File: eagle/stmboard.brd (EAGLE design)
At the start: 62.2 x 57.1 mm, 23 parts, among them IC1 LD117AS12TR

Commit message: fixed arduino header spacing
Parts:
- moved JP6 2.03 mm to (34.7, -5.71)
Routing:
- net PA10_SDA: track 42.4 -> 40.1 mm
- net GND: track 11.6 -> 13.9 mm
- net PA9_SCL_BTN: track 48.1 -> 47.3 mm
- net PA5_SCK_LED: track 50.0 -> 50.5 mm
- net PA8_PWM: track 25.7 -> 26.2 mm
- net PA7_MOSI: track 40.3 -> 40.8 mm
- net PB0_PWM: track 36.7 -> 37.3 mm
- net PA6_MISO: track 43.8 -> 44.4 mm
- net PA11: track 23.6 -> 23.1 mm
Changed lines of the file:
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@@
 <attribute name="VALUE" x="69.215" y="-2.54" size="1.27" layer="27" rot="R180"/>
 </element>
-<element name="JP6" library="pinhead" library_urn="urn:adsk.eagle:library:325" package="1X10" package3d_urn="urn:adsk.eagle:package:22406/2" value="" x="32.639" y="-5.715" locked="yes" smashed="yes" rot="R180">
-<attribute name="NAME" x="45.4152" y="-7.5438" size="1.27" layer="25" ratio="10" rot="R180"/>
-<attribute name="VALUE" x="45.339" y="-2.54" size="1.27" layer="27" rot="R180"/>
+<element name="JP6" library="pinhead" library_urn="urn:adsk.eagle:library:325" package="1X10" package3d_urn="urn:adsk.eagle:package:22406/2" value="" x="34.671" y="-5.715" smashed="yes" rot="R180">
+<attribute name="NAME" x="47.4472" y="-7.5438" size="1.27" layer="25" ratio="10" rot="R180"/>
+<attribute name="VALUE" x="47.371" y="-2.54" size="1.27" layer="27" rot="R180"/>
 </element>
 <element name="JP8" library="pinhead" library_urn="urn:adsk.eagle:library:325" package="1X05" package3d_urn="urn:adsk.eagle:package:22469/2" value="" x="52.07" y="5.08" smashed="yes" rot="R270">
@@
 <wire x1="52.07" y1="5.08" x2="49.53" y2="5.08" width="0.4572" layer="1"/>
 <via x="49.53" y="5.08" extent="1-16" drill="0.75" diameter="1.3"/>
-<via x="47.625" y="-3.81" extent="1-16" drill="0.75" diameter="1.3"/>
-<wire x1="49.53" y1="5.08" x2="47.625" y2="-3.81" width="0.4572" layer="16"/>
+<via x="48.26" y="-5.715" extent="1-16" drill="0.75" diameter="1.3"/>
 <contactref element="R3" pad="1"/>
 <contactref element="R4" pad="1"/>
 <contactref element="S1" pad="1"/>
 <via x="70.485" y="-5.715" extent="1-16" drill="0.75" diameter="1.3"/>
+<wire x1="49.53" y1="5.08" x2="48.26" y2="3.81" width="0.4572" layer="16"/>
+<wire x1="48.26" y1="3.81" x2="48.26" y2="-5.715" width="0.4572" layer="16"/>
 </signal>
 <signal name="PA4_AN">
@@
 <contactref element="U$1" pad="11"/>
 <contactref element="JP6" pad="6"/>
-<wire x1="31.369" y1="-5.715" x2="31.369" y2="-2.286" width="0.4572" layer="1"/>
-<wire x1="31.369" y1="-2.286" x2="31.75" y2="-1.905" width="0.4572" layer="1"/>
 <via x="31.75" y="-1.905" extent="1-16" drill="0.75" diameter="1.3"/>
 <via x="31.75" y="5.715" extent="1-16" drill="0.75" diameter="1.3"/>
@@
 <wire x1="31.75" y1="18.415" x2="29.362" y2="18.415" width="0.4572" layer="1"/>
 <wire x1="29.362" y1="18.415" x2="29.21" y2="18.567" width="0.4572" layer="1"/>
+<wire x1="31.75" y1="-1.905" x2="33.401" y2="-3.556" width="0.4572" layer="1"/>
+<wire x1="33.401" y1="-3.556" x2="33.401" y2="-5.715" width="0.4572" layer="1"/>
 </signal>
 <signal name="PA6_MISO">
 <contactref element="U$1" pad="12"/>
 <contactref element="JP6" pad="5"/>
-<wire x1="33.909" y1="-5.715" x2="33.909" y2="-2.286" width="0.4572" layer="1"/>
-<wire x1="34.29" y1="-1.905" x2="33.909" y2="-2.286" width="0.4572" layer="1"/>
 <via x="34.29" y="-1.905" extent="1-16" drill="0.75" diameter="1.3"/>
 <via x="34.29" y="5.715" extent="1-16" drill="0.75" diameter="1.3"/>
@@
 <wire x1="40.64" y1="25.4" x2="34.29" y2="19.05" width="0.4572" layer="1"/>
 <wire x1="34.29" y1="5.715" x2="34.29" y2="-1.905" width="0.4572" layer="16"/>
+<wire x1="34.29" y1="-1.905" x2="35.941" y2="-3.556" width="0.4572" layer="1"/>
+<wire x1="35.941" y1="-3.556" x2="35.941" y2="-5.715" width="0.4572" layer="1"/>
 </signal>
 <signal name="PA7_MOSI">
 <contactref element="U$1" pad="13"/>
 <contactref element="JP6" pad="4"/>
-<wire x1="36.449" y1="-5.715" x2="36.449" y2="-2.286" width="0.4572" layer="1"/>
-<wire x1="36.83" y1="-1.905" x2="36.449" y2="-2.286" width="0.4572" layer="1"/>
 <via x="36.83" y="-1.905" extent="1-16" drill="0.75" diameter="1.3"/>
 <via x="36.83" y="5.715" extent="1-16" drill="0.75" diameter="1.3"/>
@@
 <wire x1="48.751828125" y1="21.80248125" x2="46.424309375" y2="24.13" width="0.4572" layer="1"/>
 <wire x1="36.83" y1="5.715" x2="36.83" y2="-1.905" width="0.4572" layer="16"/>
+<wire x1="36.83" y1="-1.905" x2="38.481" y2="-3.556" width="0.4572" layer="1"/>
+<wire x1="38.481" y1="-3.556" x2="38.481" y2="-5.715" width="0.4572" layer="1"/>
 </signal>
 <signal name="PA8_PWM">
@@
 <contactref element="JP6" pad="2"/>
 <via x="41.91" y="-1.905" extent="1-16" drill="0.75" diameter="1.3"/>
-<wire x1="41.91" y1="-1.905" x2="41.529" y2="-2.286" width="0.4572" layer="1"/>
-<wire x1="41.529" y1="-2.286" x2="41.529" y2="-5.715" width="0.4572" layer="1"/>
 <wire x1="47.620459375" y1="17.428884375" x2="41.91" y2="11.718425" width="0.4572" layer="1"/>
 <wire x1="41.91" y1="11.718425" x2="41.91" y2="3.175" width="0.4572" layer="1"/>
 <via x="41.91" y="3.175" extent="1-16" drill="0.75" diameter="1.3"/>
 <wire x1="41.91" y1="3.175" x2="41.91" y2="-1.905" width="0.4572" layer="16"/>
+<wire x1="41.91" y1="-1.905" x2="43.561" y2="-3.556" width="0.4572" layer="1"/>
+<wire x1="43.561" y1="-3.556" x2="43.561" y2="-5.715" width="0.4572" layer="1"/>
 </signal>
 <signal name="PA11">
@@
 <contactref element="JP6" pad="1"/>
 <wire x1="49.317515625" y1="15.731828125" x2="45.72" y2="12.1343125" width="0.4572" layer="1"/>
-<wire x1="44.069" y1="-3.556" x2="44.069" y2="-5.715" width="0.4572" layer="1"/>
-<wire x1="45.72" y1="12.1343125" x2="45.72" y2="-1.905" width="0.4572" layer="1"/>
-<wire x1="45.72" y1="-1.905" x2="44.069" y2="-3.556" width="0.4572" layer="1"/>
+<wire x1="45.72" y1="-3.175" x2="46.101" y2="-3.556" width="0.4572" layer="1"/>
+<wire x1="46.101" y1="-3.556" x2="46.101" y2="-5.715" width="0.4572" layer="1"/>
+<wire x1="45.72" y1="12.1343125" x2="45.72" y2="-3.175" width="0.4572" layer="1"/>
 </signal>
 <signal name="PA12">
@@
 <contactref element="JP6" pad="9"/>
 <contactref element="U$1" pad="20"/>
-<wire x1="23.749" y1="-2.286" x2="23.749" y2="-5.715" width="0.4572" layer="1"/>
-<wire x1="26.035" y1="0" x2="23.749" y2="-2.286" width="0.4572" layer="1"/>
 <wire x1="48.751828125" y1="16.297515625" x2="44.45" y2="11.9956875" width="0.4572" layer="1"/>
 <wire x1="44.45" y1="1.27" x2="43.18" y2="0" width="0.4572" layer="1"/>
 <wire x1="44.45" y1="11.9956875" x2="44.45" y2="1.27" width="0.4572" layer="1"/>
-<wire x1="43.18" y1="0" x2="26.035" y2="0" width="0.4572" layer="1"/>
+<wire x1="43.18" y1="0" x2="28.575" y2="0" width="0.4572" layer="1"/>
+<wire x1="25.781" y1="-2.794" x2="25.781" y2="-5.715" width="0.4572" layer="1"/>
+<wire x1="28.575" y1="0" x2="25.781" y2="-2.794" width="0.4572" layer="1"/>
 </signal>
 <signal name="PA3_AN">
@@
 <contactref element="JP6" pad="3"/>
 <contactref element="U$1" pad="14"/>
-<wire x1="38.989" y1="-5.715" x2="38.989" y2="-2.286" width="0.4572" layer="1"/>
-<wire x1="39.37" y1="-1.905" x2="38.989" y2="-2.286" width="0.4572" layer="1"/>
 <via x="39.37" y="-1.905" extent="1-16" drill="0.75" diameter="1.3"/>
 <via x="39.37" y="5.715" extent="1-16" drill="0.75" diameter="1.3"/>
@@
 <wire x1="48.18614375" y1="21.236796875" x2="46.56294375" y2="22.859996875" width="0.4572" layer="1"/>
 <wire x1="46.56294375" y1="22.859996875" x2="46.562940625" y2="22.859996875" width="0.4572" layer="1"/>
+<wire x1="39.37" y1="-1.905" x2="41.021" y2="-3.556" width="0.4572" layer="1"/>
+<wire x1="41.021" y1="-3.556" x2="41.021" y2="-5.715" width="0.4572" layer="1"/>
 </signal>
 <signal name="PB1_AN">
@@
 <wire x1="43.18" y1="1.905" x2="42.545" y2="1.27" width="0.4572" layer="1"/>
 <wire x1="43.18" y1="11.85705625" x2="43.18" y2="1.905" width="0.4572" layer="1"/>
+<wire x1="23.495" y1="1.27" x2="23.495" y2="1.524" width="0.4572" layer="1"/>
+<wire x1="23.495" y1="1.2065" x2="23.495" y2="1.27" width="0.4572" layer="1"/>
+<wire x1="23.495" y1="1.524" x2="23.495" y2="4.47" width="0.4572" layer="1"/>
 <wire x1="42.545" y1="1.27" x2="23.495" y2="1.27" width="0.4572" layer="1"/>
-<wire x1="21.209" y1="-1.016" x2="21.209" y2="-5.715" width="0.4572" layer="1"/>
-<wire x1="23.495" y1="1.27" x2="21.209" y2="-1.016" width="0.4572" layer="1"/>
-<wire x1="23.495" y1="1.27" x2="23.495" y2="4.47" width="0.4572" layer="1"/>
+<wire x1="23.495" y1="1.2065" x2="23.241" y2="0.9525" width="0.4572" layer="1"/>
+<wire x1="23.241" y1="0.9525" x2="23.241" y2="-5.715" width="0.4572" layer="1"/>
 </signal>
 </signals>

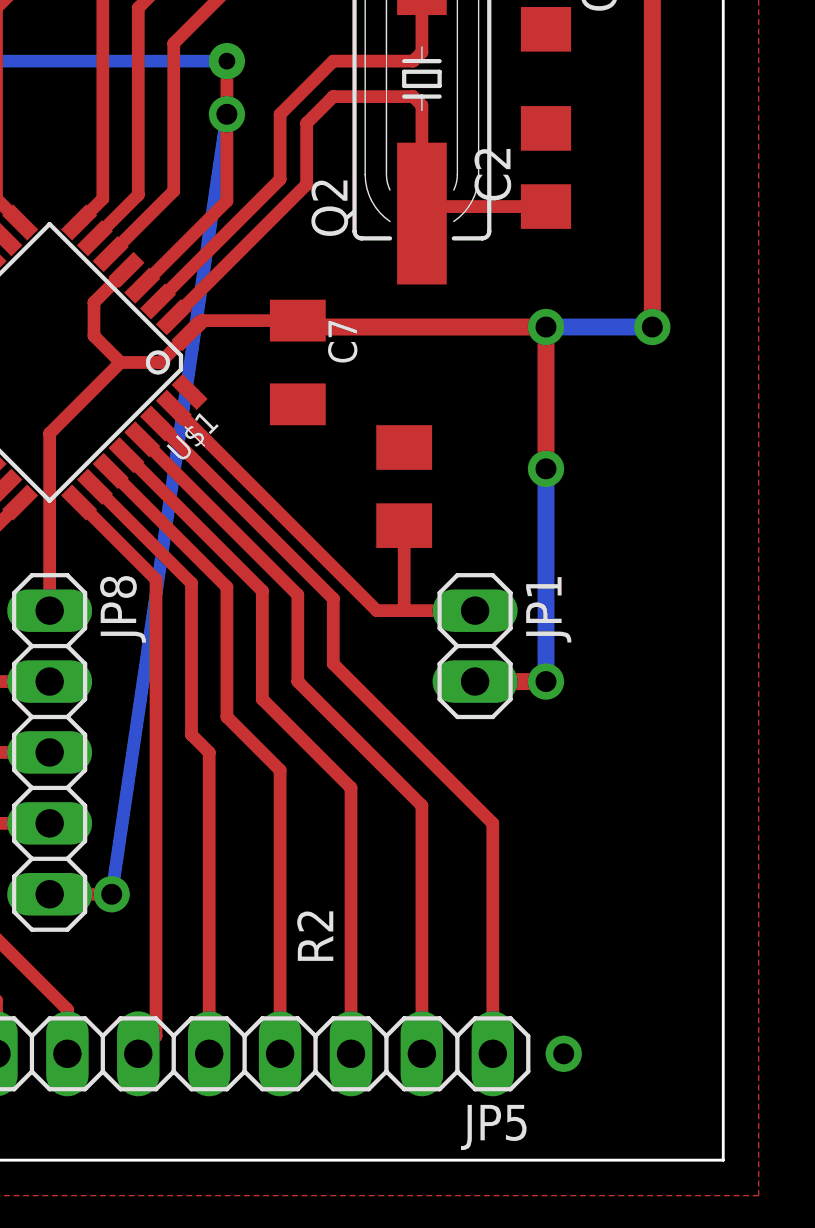
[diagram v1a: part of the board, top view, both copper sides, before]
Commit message: changed boot0 jumper to 3-pin
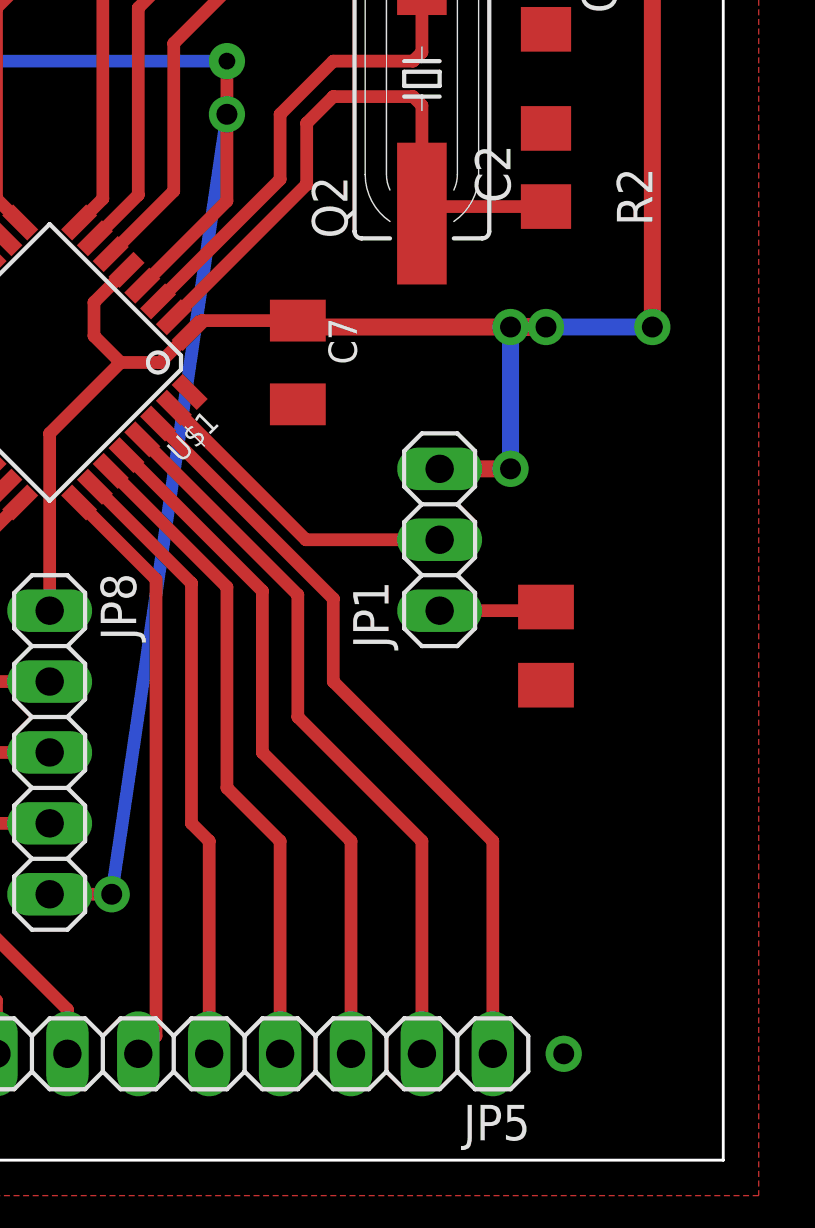
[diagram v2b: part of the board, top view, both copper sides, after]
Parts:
- JP1: device pinhead:1X02 -> pinhead:1X03
- moved R2 7.65 mm to (69.8, 8.89), turned to 270 degrees
- moved JP1 4.02 mm to (66.0, 12.7), turned to 90 degrees
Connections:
- new net N$3: JP1.1, R2.1
- net +3V3: now also JP1.3; no longer JP1.2
- net BOOT0: now also JP1.2; no longer JP1.1, R2.1
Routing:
- net +3V3: track 178.2 -> 171.9 mm
- net BOOT0: track 16.8 -> 11.5 mm
- net N$3: track 0.00 -> 3.86 mm
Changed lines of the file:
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@@
 <attribute name="VALUE" x="24.8158" y="33.02" size="1.27" layer="27" rot="R90"/>
 </element>
-<element name="R2" library="rcl" package="M1206" value="" x="64.77" y="14.605" smashed="yes" rot="R90">
-<attribute name="NAME" x="62.23" y="-2.54" size="1.27" layer="25" rot="R90"/>
-<attribute name="VALUE" x="67.31" y="13.335" size="1.27" layer="27" rot="R90"/>
+<element name="R2" library="rcl" package="M1206" value="" x="69.85" y="8.89" smashed="yes" rot="R270">
+<attribute name="NAME" x="72.39" y="26.035" size="1.27" layer="25" rot="R270"/>
+<attribute name="VALUE" x="67.31" y="10.16" size="1.27" layer="27" rot="R270"/>
 </element>
 <element name="U$1" library="stm32F030x" package="TQFP32-08" package3d_urn="urn:adsk.eagle:package:4313/2" value="STM32F030" x="52.07" y="19.05" smashed="yes" rot="R225">
@@
 <attribute name="VALUE" x="33.655" y="27.94" size="0.6096" layer="27" font="vector" ratio="20" align="top-center"/>
 </element>
-<element name="JP1" library="pinhead" library_urn="urn:adsk.eagle:library:325" package="1X02" package3d_urn="urn:adsk.eagle:package:22435/2" value="" x="67.31" y="8.89" smashed="yes" rot="R270">
-<attribute name="NAME" x="69.1388" y="11.5062" size="1.27" layer="25" ratio="10" rot="R270"/>
-<attribute name="VALUE" x="64.135" y="11.43" size="1.27" layer="27" rot="R270"/>
-</element>
 <element name="JP3" library="pinhead" library_urn="urn:adsk.eagle:library:325" package="1X08" package3d_urn="urn:adsk.eagle:package:22409/2" value="" x="40.005" y="42.545" locked="yes" smashed="yes">
 <attribute name="NAME" x="29.7688" y="44.3738" size="1.27" layer="25" ratio="10"/>
@@
 <attribute name="SF_SKU" value="COM-08229" x="13.97" y="7.62" size="1.778" layer="27" rot="R270" display="off"/>
 <attribute name="VALUE" x="12.065" y="7.62" size="0.6096" layer="27" font="vector" ratio="20" rot="R270" align="top-center"/>
+</element>
+<element name="JP1" library="pinhead" library_urn="urn:adsk.eagle:library:325" package="1X03" package3d_urn="urn:adsk.eagle:package:22458/2" value="" x="66.04" y="12.7" smashed="yes" rot="R90">
+<attribute name="NAME" x="64.2112" y="8.8138" size="1.27" layer="25" ratio="10" rot="R90"/>
+<attribute name="VALUE" x="69.215" y="8.89" size="1.27" layer="27" rot="R90"/>
 </element>
 </elements>
@@
 <contactref element="C6" pad="1"/>
 <contactref element="C7" pad="1"/>
-<contactref element="JP1" pad="2"/>
 <contactref element="JP3" pad="4"/>
 <wire x1="47.054771875" y1="17.994571875" x2="45.6577" y2="16.5975" width="0.4572" layer="1"/>
@@
 <wire x1="56.0298" y1="19.05" x2="54.610003125" y2="19.05" width="0.4572" layer="1"/>
 <wire x1="54.610003125" y1="19.05" x2="53.6575" y2="20.0025" width="0.4572" layer="1"/>
-<via x="69.85" y="7.62" extent="1-16" drill="0.75" diameter="1.3"/>
+<via x="68.58" y="15.24" extent="1-16" drill="0.75" diameter="1.3"/>
 <contactref element="JP8" pad="1"/>
 <wire x1="52.07" y1="10.16" x2="52.07" y2="16.509996875" width="0.4572" layer="1"/>
@@
 <wire x1="57.085225" y1="20.105425" x2="57.5298" y2="20.55" width="0.4572" layer="1"/>
 <wire x1="57.5298" y1="20.55" x2="60.96" y2="20.55" width="0.4572" layer="1"/>
-<via x="69.85" y="15.24" extent="1-16" drill="0.75" diameter="1.3"/>
+<via x="68.58" y="20.32" extent="1-16" drill="0.75" diameter="1.3"/>
 <wire x1="69.85" y1="20.32" x2="61.19" y2="20.32" width="0.6096" layer="1"/>
 <wire x1="61.19" y1="20.32" x2="60.96" y2="20.55" width="0.4572" layer="1"/>
-<wire x1="69.85" y1="15.24" x2="69.85" y2="20.32" width="0.6096" layer="1"/>
+<wire x1="68.58" y1="20.32" x2="69.85" y2="20.32" width="0.6096" layer="1"/>
 <contactref element="LED1" pad="A"/>
 <contactref element="C3" pad="1"/>
@@
 <wire x1="42.545" y1="28.2575" x2="42.545" y2="14.9225" width="0.6096" layer="16"/>
 <wire x1="69.85" y1="20.32" x2="73.66" y2="20.32" width="0.6096" layer="16"/>
-<wire x1="69.85" y1="15.24" x2="69.85" y2="7.62" width="0.6096" layer="16"/>
-<wire x1="67.31" y1="7.62" x2="69.85" y2="7.62" width="0.6096" layer="1"/>
+<wire x1="68.58" y1="20.32" x2="68.58" y2="15.24" width="0.6096" layer="16"/>
 <wire x1="20.725" y1="28.4875" x2="22.5425" y2="26.67" width="0.6096" layer="1"/>
 <wire x1="42.545" y1="38.1" x2="42.545" y2="28.2575" width="0.6096" layer="1"/>
 <wire x1="31.902" y1="24.13" x2="31.902" y2="26.518" width="0.6096" layer="1"/>
 <wire x1="31.902" y1="26.518" x2="31.75" y2="26.67" width="0.6096" layer="1"/>
+<contactref element="JP1" pad="3"/>
+<wire x1="66.04" y1="15.24" x2="68.58" y2="15.24" width="0.6096" layer="1"/>
 </signal>
 <signal name="!RST">
@@
 <signal name="BOOT0">
 <contactref element="U$1" pad="31"/>
-<contactref element="R2" pad="1"/>
-<contactref element="JP1" pad="1"/>
-<wire x1="63.788421875" y1="10.16" x2="64.77" y2="10.16" width="0.4572" layer="1"/>
-<wire x1="64.77" y1="10.16" x2="67.31" y2="10.16" width="0.4572" layer="1"/>
-<wire x1="64.77" y1="13.205" x2="64.77" y2="10.16" width="0.4572" layer="1"/>
-<wire x1="56.5195375" y1="17.428884375" x2="63.788421875" y2="10.16" width="0.4572" layer="1"/>
+<wire x1="56.5195375" y1="17.428884375" x2="61.248421875" y2="12.7" width="0.4572" layer="1"/>
+<contactref element="JP1" pad="2"/>
+<wire x1="61.248421875" y1="12.7" x2="66.04" y2="12.7" width="0.4572" layer="1"/>
 </signal>
 <signal name="PA10_SDA">
@@
 <wire x1="57.785" y1="-6.35" x2="57.785" y2="-5.715" width="0.4572" layer="1"/>
 <wire x1="57.15" y1="11.141571875" x2="53.6911125" y2="14.600459375" width="0.4572" layer="1"/>
-<wire x1="57.785" y1="5.08" x2="57.15" y2="5.715" width="0.4572" layer="1"/>
-<wire x1="57.785" y1="5.08" x2="57.785" y2="-5.715" width="0.4572" layer="1"/>
-<wire x1="57.15" y1="11.141571875" x2="57.15" y2="5.715" width="0.4572" layer="1"/>
+<wire x1="57.785" y1="1.905" x2="57.15" y2="2.54" width="0.4572" layer="1"/>
+<wire x1="57.785" y1="1.905" x2="57.785" y2="-5.715" width="0.4572" layer="1"/>
+<wire x1="57.15" y1="11.141571875" x2="57.15" y2="2.54" width="0.4572" layer="1"/>
 </signal>
 <signal name="PB6_TX">
@@
 <contactref element="U$1" pad="29"/>
 <wire x1="60.96" y1="10.725684375" x2="55.38816875" y2="16.297515625" width="0.4572" layer="1"/>
-<wire x1="65.405" y1="3.175" x2="60.96" y2="7.62" width="0.4572" layer="1"/>
-<wire x1="65.405" y1="3.175" x2="65.405" y2="-5.715" width="0.4572" layer="1"/>
-<wire x1="60.96" y1="10.725684375" x2="60.96" y2="7.62" width="0.4572" layer="1"/>
+<wire x1="65.405" y1="1.905" x2="60.96" y2="6.35" width="0.4572" layer="1"/>
+<wire x1="65.405" y1="1.905" x2="65.405" y2="-5.715" width="0.4572" layer="1"/>
+<wire x1="60.96" y1="10.725684375" x2="60.96" y2="6.35" width="0.4572" layer="1"/>
 </signal>
 <signal name="PB7_RX">
 <contactref element="JP5" pad="1"/>
 <contactref element="U$1" pad="30"/>
-<wire x1="67.945" y1="2.54" x2="62.23" y2="8.255" width="0.4572" layer="1"/>
-<wire x1="67.945" y1="2.54" x2="67.945" y2="-5.715" width="0.4572" layer="1"/>
-<wire x1="62.229996875" y1="10.587053125" x2="62.23" y2="8.255" width="0.4572" layer="1"/>
+<wire x1="67.945" y1="1.905" x2="62.23" y2="7.62" width="0.4572" layer="1"/>
+<wire x1="67.945" y1="1.905" x2="67.945" y2="-5.715" width="0.4572" layer="1"/>
+<wire x1="62.229996875" y1="10.587053125" x2="62.23" y2="7.62" width="0.4572" layer="1"/>
 <wire x1="55.953853125" y1="16.8632" x2="62.229996875" y2="10.58705625" width="0.4572" layer="1"/>
 <wire x1="62.229996875" y1="10.58705625" x2="62.229996875" y2="10.587053125" width="0.4572" layer="1"/>
@@
 <contactref element="JP5" pad="4"/>
 <contactref element="U$1" pad="27"/>
-<wire x1="60.325" y1="4.445" x2="58.42" y2="6.35" width="0.4572" layer="1"/>
-<wire x1="60.325" y1="4.445" x2="60.325" y2="-5.715" width="0.4572" layer="1"/>
-<wire x1="58.42" y1="11.002940625" x2="58.42" y2="6.35" width="0.4572" layer="1"/>
+<wire x1="60.325" y1="1.905" x2="58.42" y2="3.81" width="0.4572" layer="1"/>
+<wire x1="60.325" y1="1.905" x2="60.325" y2="-5.715" width="0.4572" layer="1"/>
+<wire x1="58.42" y1="11.002940625" x2="58.42" y2="3.81" width="0.4572" layer="1"/>
 <wire x1="54.256796875" y1="15.16614375" x2="58.42" y2="11.002940625" width="0.4572" layer="1"/>
 </signal>
@@
 <contactref element="U$1" pad="28"/>
 <wire x1="59.69" y1="10.864309375" x2="54.82248125" y2="15.731828125" width="0.4572" layer="1"/>
-<wire x1="62.865" y1="3.81" x2="59.69" y2="6.985" width="0.4572" layer="1"/>
-<wire x1="62.865" y1="3.81" x2="62.865" y2="-5.715" width="0.4572" layer="1"/>
-<wire x1="59.69" y1="10.864309375" x2="59.69" y2="6.985" width="0.4572" layer="1"/>
+<wire x1="62.865" y1="1.905" x2="59.69" y2="5.08" width="0.4572" layer="1"/>
+<wire x1="62.865" y1="1.905" x2="62.865" y2="-5.715" width="0.4572" layer="1"/>
+<wire x1="59.69" y1="10.864309375" x2="59.69" y2="5.08" width="0.4572" layer="1"/>
 </signal>
 <signal name="N$1">
@@
 <wire x1="23.241" y1="0.9525" x2="23.241" y2="-5.715" width="0.4572" layer="1"/>
 </signal>
+<signal name="N$3">
+<contactref element="JP1" pad="1"/>
+<contactref element="R2" pad="1"/>
+<wire x1="69.85" y1="10.29" x2="69.72" y2="10.16" width="0.4572" layer="1"/>
+<wire x1="69.72" y1="10.16" x2="66.04" y2="10.16" width="0.4572" layer="1"/>
+</signal>
 </signals>
